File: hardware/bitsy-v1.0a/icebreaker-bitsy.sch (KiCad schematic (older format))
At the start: 100 parts, among them J1 Conn_01x01, J10 Conn_01x01, J11 Conn_01x01, J12 Conn_01x01, J13 Conn_01x01, J14 Conn_01x01, J15 Conn_01x01, J16 Conn_01x01, J17 Conn_01x01, J18 Conn_01x01, J19 Conn_01x01, J2 Conn_01x01, J20 Conn_01x01, J21 Conn_01x01, J22 Conn_01x01, J23 Conn_01x01, J24 Conn_01x01, J25 Conn_01x01, J26 Conn_01x01, J27 Conn_01x01, J28 Conn_01x01, J29 Conn_01x01, J3 Conn_01x01, J30 Conn_01x01, J31 Conn_01x01, J32 Conn_01x01, J33 Conn_01x01, J34 Conn_01x01, J35 Conn_01x01, J36 Conn_01x01, J37 Conn_01x01, J38 Conn_01x01, J39 Conn_01x01, J4 Conn_01x01, J40 Conn_01x01, J5 Conn_01x01, J6 Conn_01x01, J7 Conn_01x01, J8 Conn_01x01, J9 Conn_01x01, P1 USB_C, P2 UP, P3 UP, P4 UP, P5 UP, SW1 TACT, U1 USBLC6-2, U2 TLV75533PDRV, U3 TLV75512PDRV, U4 LY68L6400, U5 W25Q, U6 ICE40UP5K-SG48, X1 DSC6101CI1A-012.0000T

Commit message: WIP placement
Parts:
- removed C27, C30, C31: 100n, pkl_dipol:C_0402, symbol pkl_device:pkl_C_Small
- removed J24, J25: Conn_01x01, pkl_pin_headers:Pin_Header_Straight_Round_1x01, symbol Connector_Generic:Conn_01x01
- removed JP7, JP8, JP9: Jumper, pkl_jumpers:J_NC_0603_30, symbol pkl_misc:pkl_jumper_nc
- added C17, C18, C19: 100n, pkl_dipol:C_0402, symbol pkl_device:pkl_C_Small
- D4: renamed from D1; value FC-B1010RGBT-HG -> FM-B2020RGBA-HG; footprint pkl_led:LED_TRI_1010 -> pkl_led:LED_TRI_2020
- renumbered C8 to C1, C35 to C10, C23 to C11, C25 to C12, C28 to C13, C36 to C14, C37 to C15, C38 to C16, C15 to C2, C39 to C3, C2 to C4, C22 to C6, C4 to C7, C24 to C8, C26 to C9, D5 to D1, D4 to D2, J27 to J24, J28 to J25, J29 to J27, J30 to J28, J31 to J29, J32 to J30, J39 to J31, J40 to J32, JP6 to JP2, JP5 to JP3, JP3 to JP5, JP2 to JP6, R19 to R11, R13 to R12, R15 to R13, R12 to R15, R5 to R2, R8 to R3, R6 to R5, R2 to R6, R3 to R7, R11 to R8, R7 to R9, U3 to U2, U2 to U3
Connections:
- net ~LED_GRN is gone; now on net ~RGB1: U6.40 (RGB1)
- net ~LED_RED is gone; now on net ~RGB0: U6.39 (RGB0)
- net +1V2: no longer J3.1 (Pin_1)
- net +3V3: now also R15.2; no longer R15.1
- net GND: now also J4.1 (Pin_1), C17.2, C18.2, C19.2
- net ICEVCC: now also R10.1; no longer R10.2
- net VCCIO_01: now also C17.1, C18.1
- net VCCIO_2: now also C19.1
- net VIN: now also J3.1 (Pin_1); no longer J4.1 (Pin_1)
- net iCE_CDONE: now also R15.1; no longer R15.2
- net VPP_2V5: now reaches C10.1, JP3.2, U6.24 (VPP_2V5)
- net VCCPLL: now reaches C8.1, C9.1, U6.29 (VCCPLL)
- net VCCPLL: now also R10.2; no longer R10.1
- net CLK_EN: now reaches R9.2, X1.1 (EN)
- net 3V3_EN: now reaches C3.1, R7.2, U3.4 (EN)
- net ~RGB2: now reaches D4.2 (RK)
- net ~RGB2: now also U6.41 (RGB2)
- net ~RGB1: now reaches D4.3 (GK)
- net ~RGB0: now reaches D4.4 (BK)
- net FLASH_~HLD~-~RST~-IO3 renamed FLASH_~HLD~-IO3
- net iUD+ renamed iD+
- net iUD- renamed iD-
- net xUD+ renamed xD+
- net xUD- renamed xD-
- net ~BUTTON renamed ~UBTN
- net ~LEDG renamed RAM_SS-~LEDG
- net ~LEDR renamed IOB_20A-~LEDR
- net IOB_20A-~LEDR: now also J26.1 (Pin_1)
- removed net ~LED_BLU: J26.1 (Pin_1), U6.41 (RGB2)
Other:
- note added: "Button"
- note added: "Enable Delay\n~~0.001s\nShould enable\nafter 1V2 rail"
- note added: "External Clock"
- note added: "Flash/RAM"
- note added: "JP2: Remove jumper when only programming iCE\nReplace jumper for programming Flash and for normal operation"
- note added: "LEDs"
- note added: "Power\nPins"
- note added: "TODO: fix symbol pinout"
- note added: "or less"
- note removed: "10k or less"
- note removed: "Enable Delay\n~~0.001s\nShould enable\nafter 1v2 rail\n(Test!!!)"
- note removed: "Ext Clock"
- note removed: "J18: Remove jumper when only programming iCE\nReplace jumper for programming Flash and for normal operation"
- note removed: "LED/BTN"
- note removed: "iCE FPGA Flash/Ram"
- note removed: "iCE FPGA Flash\n& Prog Pins"
- moved on the sheet: C1, C10, C11, C12, C13, C14, C15, C16, C2, C3, C4, C5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

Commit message: Programming header ideas
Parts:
- removed J33, J34, J35, J36, J37, J38: Conn_01x01, pkl_pin_headers:Pin_Header_Straight_Round_1x01, symbol Connector_Generic:Conn_01x01
- added P10, P5, P6, P7, P8, P9: POGO_PAD_SMD, pkl_pads:POGO_PAD_SMD_R_1x1, symbol pkl_misc:POGO_PAD_SMD
- renumbered P1 to J34, P2 to P1, P3 to P2, P4 to P3, P5 to P4
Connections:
- net FLASH_MISO-IO1: now also P8.1 (PAD)
- net FLASH_MOSI-IO0: now also P7.1 (PAD)
- net FLASH_~HLD~-IO3: now also P10.1 (PAD)
- net FLASH_~WP~-IO2: now also P9.1 (PAD)
- net iCE_SCK: now also P6.1 (PAD)
- net iCE_SS_B: now also P5.1 (PAD)

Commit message: Tentatively finished component placement
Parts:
- removed P10, P5, P6, P7, P8, P9: POGO_PAD_SMD, pkl_pads:POGO_PAD_SMD_R_1x1, symbol pkl_misc:POGO_PAD_SMD
- added J33: Conn_02x05_Odd_Even, Connector_PinHeader_2.54mm:PinHeader_2x05_P2.54mm_Vertical_SMD, symbol Connector_Generic:Conn_02x05_Odd_Even
- D4: symbol Device:LED_ARGB -> pkl_device:pkl_LED_RBAG
- U5: footprint pkl_housings_soic:SOIC-8_5.3x5.3mm_Pitch1.27mm -> Package_SO:SOIC-8_5.275x5.275mm_P1.27mm
- X1: value DSC6101CI1A-012.0000T -> 12MHz
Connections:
- net +3V3: now also D4.3 (A), R11.2, J33.7 (Pin_7); no longer D4.1 (A), R11.1
- net FLASH_MISO-IO1: now also J33.9 (Pin_9)
- net FLASH_MOSI-IO0: now also J33.6 (Pin_6)
- net FLASH_~HLD~-IO3: now also J33.8 (Pin_8)
- net FLASH_~WP~-IO2: now also J33.10 (Pin_10)
- net GND: now also J33.5 (Pin_5)
- net iCE_CDONE: now also J33.1 (Pin_1)
- net iCE_CRESET: now also R11.1, J33.3 (Pin_3); no longer R11.2
- net iCE_SCK: now also J33.4 (Pin_4)
- net iCE_SS_B: now also J33.2 (Pin_2)
- net ~RGB0: now also D4.1 (RK); no longer D4.4 (BK)
- net ~RGB1: now also D4.4 (GK); no longer D4.3 (GK)
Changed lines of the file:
@@
 F 0 "U5" H 1750 2050 50  0000 C CNN
 F 1 "W25Q" H 1800 1950 50  0000 C CNN
-F 2 "pkl_housings_soic:SOIC-8_5.3x5.3mm_Pitch1.27mm" H 1700 2000 50  0001 C CNN
+F 2 "Package_SO:SOIC-8_5.275x5.275mm_P1.27mm" H 1700 2000 50  0001 C CNN
 F 3 "" H 1700 2000 50  0001 C CNN
 F 4 "ANY" H 1700 2000 50  0001 C CNN "Source"
@@
 U 1 1 5AA4ED06
 P 5400 6800
-F 0 "R11" V 5300 6800 50  0000 C CNN
-F 1 "10k" V 5500 6800 50  0000 C CNN
+F 0 "R11" V 5500 6800 50  0000 C CNN
+F 1 "10k" V 5300 6800 50  0000 C CNN
 F 2 "pkl_dipol:R_0402" H 5459 6707 60  0001 L CNN
 F 3 "" H 5400 6800 60  0000 C CNN
@@
 F 5 "res-0402-10k" H -5800 1400 50  0001 C CNN "Key"
 	1    5400 6800
-	1    0    0    -1
+	-1   0    0    1
 $EndComp
 $Comp
@@
 	14050 4650 12850 4650
 Wire Notes Line
-	600  600  4700 600
+	600  600  4200 600
 Wire Notes Line
 	600  2700 600  600
 Wire Notes Line
-	4700 600  4700 2700
+	4200 600  4200 2700
 Wire Wire Line
 	13950 7700 14050 7700
@@
 P 13650 7700
 F 0 "X1" H 13450 7950 50  0000 L CNN
-F 1 "DSC6101CI1A-012.0000T" H 12600 7450 50  0000 L CNN
+F 1 "12MHz" H 13750 7950 50  0000 L CNN
 F 2 "pkl_misc:Oscillator_SMD_SCTF_S2DXX-4Pin_2.5x2.0mm" H 14350 7350 50  0001 C CNN
 F 3 "" H 13550 7700 50  0001 C CNN
@@
 $EndComp
 Wire Wire Line
-	2800 1900 4100 1900
-Wire Wire Line
-	3650 1800 4100 1800
-Wire Wire Line
-	2700 2000 4100 2000
-Wire Wire Line
-	2600 2100 4100 2100
-Wire Wire Line
-	2500 2200 4100 2200
-Wire Wire Line
-	2400 2300 4100 2300
+	2800 1900 3000 1900
+Wire Wire Line
+	3650 1800 3750 1800
+Wire Wire Line
+	2700 2000 3000 2000
+Wire Wire Line
+	2600 2100 3000 2100
+Wire Wire Line
+	2500 2200 3000 2200
+Wire Wire Line
+	2400 2300 3000 2300
 $Comp
 L power:GND #PWR045
@@
 $EndComp
 Wire Notes Line
-	4700 2700 600  2700
+	4200 2700 600  2700
 Connection ~ 2900 1800
 Connection ~ -1550 6000
@@
 Wire Wire Line
 	-1650 7000 -1550 7000
-$Comp
-L Device:LED_ARGB D4
-U 1 1 5EDC5897
-P -1850 7000
-F 0 "D4" H -1850 6650 50  0000 C CNN
-F 1 "FM-B2020RGBA-HG" H -1850 7400 50  0000 C CNN
-F 2 "pkl_led:LED_TRI_2020" H -1850 6950 50  0001 C CNN
-F 3 "~" H -1850 6950 50  0001 C CNN
-F 4 "led-1010-rgb" H -1850 7000 50  0001 C CNN "Key"
-	1    -1850 7000
-	1    0    0    1
-$EndComp
 Text Label -2150 6800 2    50   ~ 0
 ~RGB0
@@
 $EndComp
 $Comp
-L pkl_misc:POGO_PAD_SMD P5
-U 1 1 5ED048A1
-P 4300 1800
-F 0 "P5" H 4378 1795 60  0000 L CNN
-F 1 "POGO_PAD_SMD" H 4378 1742 60  0001 L CNN
-F 2 "pkl_pads:POGO_PAD_SMD_R_1x1" H 4300 1550 60  0001 C CNN
-F 3 "" H 4300 1650 60  0000 C CNN
-	1    4300 1800
-	1    0    0    -1
-$EndComp
-$Comp
-L pkl_misc:POGO_PAD_SMD P6
-U 1 1 5ED3CC0E
-P 4300 1900
-F 0 "P6" H 4378 1895 60  0000 L CNN
-F 1 "POGO_PAD_SMD" H 4378 1842 60  0001 L CNN
-F 2 "pkl_pads:POGO_PAD_SMD_R_1x1" H 4300 1650 60  0001 C CNN
-F 3 "" H 4300 1750 60  0000 C CNN
-	1    4300 1900
-	1    0    0    -1
-$EndComp
-$Comp
-L pkl_misc:POGO_PAD_SMD P7
-U 1 1 5ED3CDEF
-P 4300 2000
-F 0 "P7" H 4378 1995 60  0000 L CNN
-F 1 "POGO_PAD_SMD" H 4378 1942 60  0001 L CNN
-F 2 "pkl_pads:POGO_PAD_SMD_R_1x1" H 4300 1750 60  0001 C CNN
-F 3 "" H 4300 1850 60  0000 C CNN
-	1    4300 2000
-	1    0    0    -1
-$EndComp
-$Comp
-L pkl_misc:POGO_PAD_SMD P8
-U 1 1 5ED3CFD9
-P 4300 2100
-F 0 "P8" H 4378 2095 60  0000 L CNN
-F 1 "POGO_PAD_SMD" H 4378 2042 60  0001 L CNN
-F 2 "pkl_pads:POGO_PAD_SMD_R_1x1" H 4300 1850 60  0001 C CNN
-F 3 "" H 4300 1950 60  0000 C CNN
-	1    4300 2100
-	1    0    0    -1
-$EndComp
-$Comp
-L pkl_misc:POGO_PAD_SMD P9
-U 1 1 5ED3D1F2
-P 4300 2200
-F 0 "P9" H 4378 2195 60  0000 L CNN
-F 1 "POGO_PAD_SMD" H 4378 2142 60  0001 L CNN
-F 2 "pkl_pads:POGO_PAD_SMD_R_1x1" H 4300 1950 60  0001 C CNN
-F 3 "" H 4300 2050 60  0000 C CNN
-	1    4300 2200
-	1    0    0    -1
-$EndComp
-$Comp
-L pkl_misc:POGO_PAD_SMD P10
-U 1 1 5ED3D3C3
-P 4300 2300
-F 0 "P10" H 4378 2295 60  0000 L CNN
-F 1 "POGO_PAD_SMD" H 4378 2242 60  0001 L CNN
-F 2 "pkl_pads:POGO_PAD_SMD_R_1x1" H 4300 2050 60  0001 C CNN
-F 3 "" H 4300 2150 60  0000 C CNN
-	1    4300 2300
-	1    0    0    -1
-$EndComp
+L pkl_device:pkl_LED_RBAG D4
+U 1 1 5EDC5897
+P -1850 7000
+F 0 "D4" H -1850 7400 50  0000 C CNN
+F 1 "FM-B2020RGBA-HG" H -1850 6650 50  0000 C CNN
+F 2 "pkl_led:LED_TRI_2020" H -1850 6950 50  0001 C CNN
+F 3 "~" H -1850 6950 50  0001 C CNN
+F 4 "led-1010-rgb" H -1850 7000 50  0001 C CNN "Key"
+	1    -1850 7000
+	1    0    0    -1
+$EndComp
+$Comp
+L Connector_Generic:Conn_02x05_Odd_Even J33
+U 1 1 5EF51AE9
+P 5950 1950
+F 0 "J33" H 6000 2367 50  0000 C CNN
+F 1 "Conn_02x05_Odd_Even" H 6000 2276 50  0000 C CNN
+F 2 "Connector_PinHeader_2.54mm:PinHeader_2x05_P2.54mm_Vertical_SMD" H 5950 1950 50  0001 C CNN
+F 3 "~" H 5950 1950 50  0001 C CNN
+	1    5950 1950
+	1    0    0    -1
+$EndComp
+Text Label 5650 1750 2    50   ~ 0
+iCE_CDONE
+Wire Wire Line
+	5750 1750 5650 1750
+Text Label 5650 1850 2    50   ~ 0
+iCE_CRESET
+Wire Wire Line
+	5750 1850 5650 1850
+$Comp
+L power:GND #PWR0120
+U 1 1 5EFA44D2
+P 5750 1950
+F 0 "#PWR0120" H 5750 1700 50  0001 C CNN
+F 1 "GND" V 5755 1822 50  0000 R CNN
+F 2 "" H 5750 1950 50  0001 C CNN
+F 3 "" H 5750 1950 50  0001 C CNN
+	1    5750 1950
+	0    1    1    0
+$EndComp
+$Comp
+L power:+3.3V #PWR0121
+U 1 1 5EFA60B8
+P 5750 2050
+F 0 "#PWR0121" H 5750 1900 50  0001 C CNN
+F 1 "+3.3V" V 5765 2178 50  0000 L CNN
+F 2 "" H 5750 2050 50  0001 C CNN
+F 3 "" H 5750 2050 50  0001 C CNN
+	1    5750 2050
+	0    -1   -1   0
+$EndComp
+Text Label 5650 2150 2    50   ~ 0
+FLASH_MISO-IO1
+Wire Wire Line
+	5750 2150 5650 2150
+Text Label 6350 2150 0    50   ~ 0
+FLASH_~WP~-IO2
+Wire Wire Line
+	6250 2150 6350 2150
+Wire Wire Line
+	6250 2050 6350 2050
+Wire Wire Line
+	6250 1950 6350 1950
+Wire Wire Line
+	6250 1850 6350 1850
+Wire Wire Line
+	6250 1750 6350 1750
+Text Label 6350 2050 0    50   ~ 0
+FLASH_~HLD~-IO3
+Text Label 6350 1950 0    50   ~ 0
+FLASH_MOSI-IO0
+Text Label 6350 1850 0    50   ~ 0
+iCE_SCK
+Text Label 6350 1750 0    50   ~ 0
+iCE_SS_B
 $EndSCHEMATC

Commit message: Begin routing
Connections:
- net ICEVCC: now also R10.2; no longer R10.1
- net VCCPLL: now also R10.1; no longer R10.2
- net ~RGB0: now also D4.2 (BK); no longer D4.1 (RK)
- net ~RGB2: now also D4.1 (RK); no longer D4.2 (BK)
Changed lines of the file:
@@
 U 1 1 5A87208D
 P 1600 6800
-F 0 "R10" V 1550 6650 50  0000 C CNN
-F 1 "100E" V 1550 7000 50  0000 C CNN
+F 0 "R10" V 1650 6950 50  0000 C CNN
+F 1 "100E" V 1650 6600 50  0000 C CNN
 F 2 "pkl_dipol:R_0402" H 1659 6707 60  0001 L CNN
 F 3 "" H 1600 6800 60  0000 C CNN
@@
 F 5 "res-0402-100" H -5750 1100 50  0001 C CNN "Key"
 	1    1600 6800
-	0    1    1    0
+	0    -1   -1   0
 $EndComp
 Wire Wire Line
@@
 Wire Wire Line
 	-1650 7000 -1550 7000
-Text Label -2150 6800 2    50   ~ 0
+Text Label -2150 7200 2    50   ~ 0
 ~RGB0
 Text Label -2150 7000 2    50   ~ 0
 ~RGB1
-Text Label -2150 7200 2    50   ~ 0
-~RGB2
 Wire Wire Line
 	-2150 6800 -2050 6800
@@
 Text Label 6350 1750 0    50   ~ 0
 iCE_SS_B
+Text Label -2150 6800 2    50   ~ 0
+~RGB2
 $EndSCHEMATC

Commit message: Routing WIP
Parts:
- added C7: 100n, pkl_dipol:C_0402, symbol pkl_device:pkl_C_Small
- renumbered C17 to C10, C18 to C11, C19 to C12, C16 to C13, C15 to C14, C14 to C15, C13 to C16, C12 to C17, C11 to C18, C9 to C19, C8 to C20, C7 to C8, C10 to C9
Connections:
- net +3V3: now also C7.1
- net FLASH_SS: now also R8.4; no longer R8.2
- net FLASH_~HLD~-IO3: now also R8.2; no longer R8.4
- net FLASH_~WP~-IO2: now also R8.8; no longer R8.6
- net GND: now also C7.2
- net iCE_SCK: now also R8.6; no longer R8.8
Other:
- moved on the sheet: R8A, R8B, R8C, R8D

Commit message: Almost done routing!
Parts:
- added JP6: Jumper, pkl_jumpers:J_NC_0603_30, symbol pkl_misc:pkl_jumper_nc
- added LOGO1: 1BitSquared, pkl_logos:null_Logo_SilkS_6.5mm, symbol pkl_logos:1BitSquared
- J1, J2: value Conn_01x01 -> 3V3
- J10: value Conn_01x01 -> 4
- J11: value Conn_01x01 -> 1
- J12: value Conn_01x01 -> 5
- J13: value Conn_01x01 -> 7
- J14: value Conn_01x01 -> 6
- J15: value Conn_01x01 -> 16
- J16: value Conn_01x01 -> 15
- J17: value Conn_01x01 -> 18
- J18: value Conn_01x01 -> 17
- J19: value Conn_01x01 -> 19
- J20: value Conn_01x01 -> 20
- J21: value Conn_01x01 -> 21
- J22: value Conn_01x01 -> 22
- J23: value Conn_01x01 -> 23
- J24: value Conn_01x01 -> 8
- J25: value Conn_01x01 -> 9
- J26: value Conn_01x01 -> 13
- J27: value Conn_01x01 -> 14
- J28: value Conn_01x01 -> 12
- J29: value Conn_01x01 -> 11
- J3: value Conn_01x01 -> VIN
- J30: value Conn_01x01 -> 10
- J31: value Conn_01x01 -> CDONE
- J32: value Conn_01x01 -> CRESET
- J34: renamed from J33; value Conn_02x05_Odd_Even -> PROG; footprint Connector_PinHeader_2.54mm:PinHeader_2x05_P2.54mm_Vertical_SMD -> pkl_pin_headers:PinHeader_2x05_P2.54mm_Vertical_SMD
- J4, J5, J6: value Conn_01x01 -> GND
- J7: value Conn_01x01 -> 2
- J8: value Conn_01x01 -> 3
- J9: value Conn_01x01 -> 0
- P1, P2, P3, P4: footprint pkl_pads:PAD_SMD_1x2.65 -> pkl_pads:PAD_SMD_1x2.65_ROUNDED
- renumbered J34 to J33, JP6 to JP7
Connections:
- net +3V3: now also JP6.2
- net FLASH_MISO-IO1: now also J34.6 (Pin_6); no longer J34.9 (Pin_9)
- net FLASH_MOSI-IO0: now also J34.8 (Pin_8); no longer J34.6 (Pin_6)
- net FLASH_~HLD~-IO3: now also J34.10 (Pin_10); no longer J34.8 (Pin_8)
- net FLASH_~WP~-IO2: now also J34.9 (Pin_9); no longer J34.10 (Pin_10)
- net ICEVCC renamed VCC
- net VCCIO_01 renamed VCCIO_0
- net VCCIO_0: no longer C11.1, U6.22 (SPI_VCCIO1)
- new net VCCIO_1: C11.1, JP6.1, U6.22 (SPI_VCCIO1)
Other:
- moved on the sheet: JP5, JP7

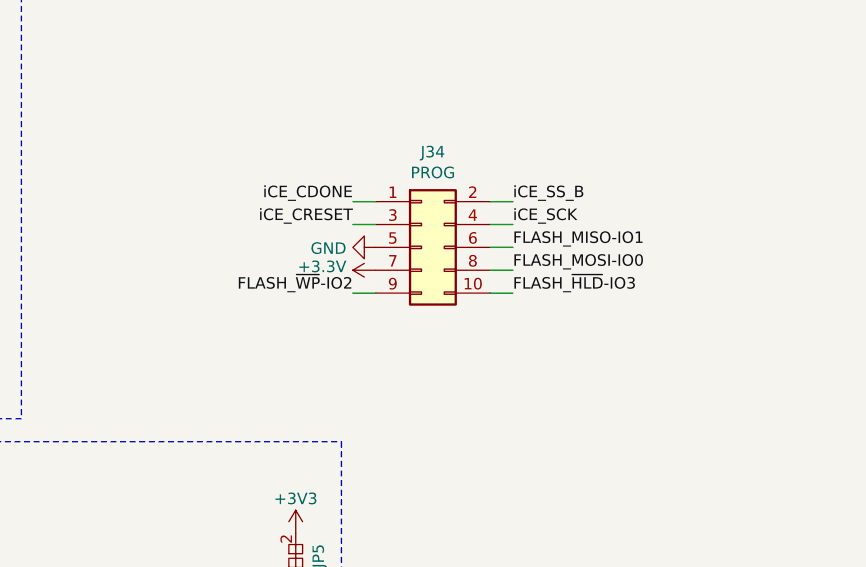
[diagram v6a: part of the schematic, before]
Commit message: One net left to route
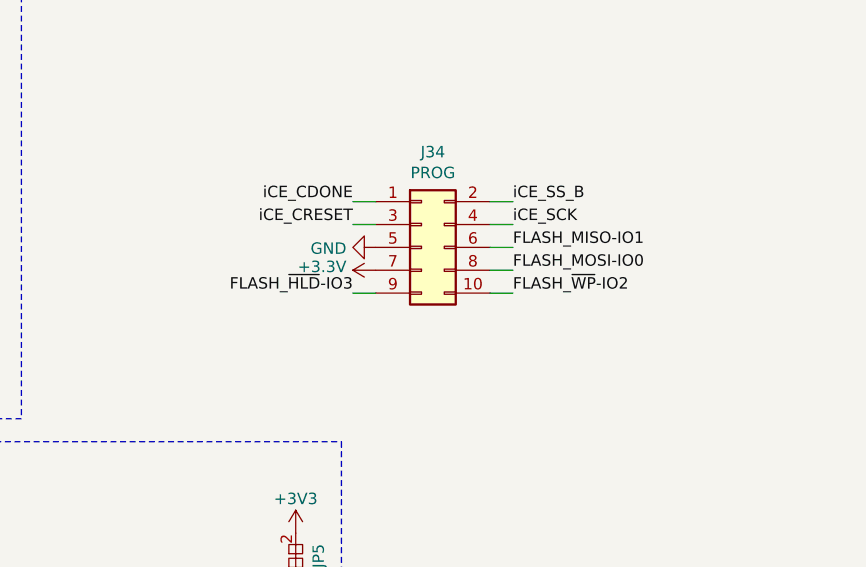
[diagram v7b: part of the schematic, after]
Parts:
- J1, J10, J11, J12, J13, J14, J15, J16, J17, J18, J19, J2, J20, J21, J22, J23, J24, J25, J26, J27, J28, J29, J3, J30, J31, J32, J4, J5, J6, J7, J8, J9: footprint pkl_pin_headers:Pin_Header_Straight_Round_1x01 -> pkl_pin_headers:Pin_Header_Straight_Round_1x01_Castellated
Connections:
- net FLASH_~HLD~-IO3: now also J34.9 (Pin_9); no longer J34.10 (Pin_10)
- net FLASH_~WP~-IO2: now also J34.10 (Pin_10); no longer J34.9 (Pin_9)

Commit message: Finish routing bitsy-v1.0a
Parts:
- added JP2: Jumper, pkl_jumpers:J_NC_0402_15, symbol pkl_misc:pkl_jumper_nc
- C9: value DNP -> 100n
- JP1: footprint pkl_jumpers:J_NC_0603_30 -> pkl_jumpers:J_NC_0603_20x2
- JP4: renamed from JP3; footprint pkl_jumpers:J_NC_0402_15 -> pkl_jumpers:J_NC_0402_30
- JP5: renamed from JP4; footprint pkl_jumpers:J_NC_0603_30 -> pkl_jumpers:J_NC_0603_20x2
- LOGO1: footprint pkl_logos:null_Logo_SilkS_6.5mm -> pkl_logos:1b2_Logo_SilkS_6.5mm
- renumbered JP2 to JP3, JP5 to JP6, JP6 to JP7, JP7 to JP8
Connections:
- net IOB_20A-~LEDR renamed ~LEDR
- net RAM_SS-~LEDG renamed ~LEDG
- net ~LEDG: now also JP2.2; no longer U4.1 (~CE)
- new net RAM_SS: JP2.1, U4.1 (~CE)
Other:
- note added: "Programming"
- note removed: "TBD: connect to VIN or VBUS?"
- note removed: "TODO: fix symbol pinout"
- moved on the sheet: C1, C10, C11, C12, C13, C14, C15, C16, C17, C18, C19, C2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
